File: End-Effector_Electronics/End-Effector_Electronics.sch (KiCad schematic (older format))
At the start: 23 parts, among them J1 Raspberry_Pi_2_3, J2 LynxServo, J3 QWIIC_Generic_Conn, J4 LynxServo, Q1 Q_PMOS_GSD, Q2 DMMT3906, Q3 Q_NMOS_GSD, U2 CAT24C32, U3 TDK_I3A4W008A033V

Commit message: Worked on finding components
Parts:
- C1: renamed from C5; footprint (none) -> Capacitor_SMD:CP_Elec_6.3x5.4; Digikey Part Num (none) -> PCE4244CT-ND
- C2: renamed from C6; footprint (none) -> Capacitor_SMD:C_0603_1608Metric
- C3: renamed from C7; footprint (none) -> Capacitor_SMD:CP_Elec_6.3x5.4; Digikey Part Num (none) -> 493-9805-1-ND
- H1, H2, H3, H4: footprint (none) -> MountingHole:MountingHole_2.7mm_M2.5_Pad
- renumbered J4 to J3, J3 to J4, R3 to R1, R4 to R2, R5 to R3, R6 to R4, R1 to R5, R2 to R6, U2 to U1, U3 to U2
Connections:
- net 12V_Disable: now also J1.36 (GPIO16)

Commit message: More component part selection
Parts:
- Q1: footprint (none) -> Package_TO_SOT_SMD:SOT-23
- Q2: footprint (none) -> Package_TO_SOT_SMD:SOT-23-6
- U1: footprint (none) -> Package_SO:TSSOP-8_4.4x3mm_P0.65mm
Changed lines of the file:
@@
 F 0 "U1" H 2950 7050 50  0000 C CNN
 F 1 "CAT24C32" H 2950 6950 50  0000 C CNN
-F 2 "" H 3250 6700 50  0001 C CNN
+F 2 "Package_SO:TSSOP-8_4.4x3mm_P0.65mm" H 3250 6700 50  0001 C CNN
 F 3 "http://ww1.microchip.com/downloads/en/DeviceDoc/21703d.pdf" H 3250 6700 50  0001 C CNN
 F 4 "CAT24C32YI-GT3OSCT-ND" H 3250 6700 50  0001 C CNN "Digikey Part Num"
@@
 F 0 "Q2" H 5113 6704 50  0000 R CNN
 F 1 "DMMT3906" H 5113 6795 50  0000 R CNN
-F 2 "" H 5400 6750 50  0001 C CIN
+F 2 "Package_TO_SOT_SMD:SOT-23-6" H 5400 6750 50  0001 C CIN
 F 3 "~" H 5500 6750 50  0001 L CNN
 F 4 "DMMT3906-7-FDICT-ND" H 5400 6750 50  0001 C CNN "Digikey Part Num"
@@
 F 0 "Q1" V 5742 6200 50  0000 C CNN
 F 1 "Q_PMOS_GSD" V 5651 6200 50  0000 C CNN
-F 2 "" H 5600 6300 50  0001 C CNN
+F 2 "Package_TO_SOT_SMD:SOT-23" H 5600 6300 50  0001 C CNN
 F 3 "~" H 5400 6200 50  0001 C CNN
 F 4 "TSM500P02CXRFGCT-ND" V 5400 6200 50  0001 C CNN "Digikey Part Num"

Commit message: Update End-Effector_Electronics.sch
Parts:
- J1: footprint (none) -> Connector_PinSocket_2.54mm:PinSocket_2x20_P2.54mm_Vertical; Digikey Part Num (none) -> 1528-1785-ND
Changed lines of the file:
@@
 F 0 "J1" H 2500 3950 50  0000 C CNN
 F 1 "Raspberry_Pi_2_3" H 2800 3850 50  0000 C CNN
-F 2 "" H 2150 2600 50  0001 C CNN
+F 2 "Connector_PinSocket_2.54mm:PinSocket_2x20_P2.54mm_Vertical" H 2150 2600 50  0001 C CNN
 F 3 "https://www.raspberrypi.org/documentation/hardware/raspberrypi/schematics/rpi_SCH_3bplus_1p0_reduced.pdf" H 2150 2600 50  0001 C CNN
+F 4 "1528-1785-ND" H 2150 2600 50  0001 C CNN "Digikey Part Num"
 	1    2150 2600
 	1    0    0    -1

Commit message: finished associating part nums and footprints
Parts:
- BT1: footprint (none) -> Connector_AMASS:AMASS_XT30PW-M_1x02_P2.50mm_Horizontal; Digikey Part Num (none) -> n/a
- H1, H2, H3, H4: Digikey Part Num (none) -> n/a
- J4: footprint (none) -> Connector_JST:JST_SH_BM04B-SRSS-TB_1x04-1MP_P1.00mm_Vertical; Digikey Part Num (none) -> n/a
- Q3: footprint (none) -> Package_TO_SOT_SMD:SOT-23; Digikey Part Num (none) -> DMN2041L-7DICT-ND
- R1, R2, R3: footprint (none) -> Resistor_SMD:R_0603_1608Metric
- R4: footprint (none) -> Resistor_SMD:R_0603_1608Metric; Digikey Part Num (none) -> 311-47.0KHRCT-ND
- R5: footprint (none) -> Resistor_SMD:R_0603_1608Metric; Digikey Part Num (none) -> 311-100KHRCT-ND
- R6: footprint (none) -> Resistor_SMD:R_0603_1608Metric; Digikey Part Num (none) -> RMCF0603FT1K82CT-ND
- U2: footprint (none) -> ASTRA_Footprints:Power_Supply_32nd_Brick; Digikey Part Num (none) -> I3A4W008A033V-001-R
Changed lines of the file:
@@
 F 0 "U2" H 7950 4765 50  0000 C CNN
 F 1 "TDK_I3A4W008A033V" H 7950 4674 50  0000 C CNN
-F 2 "" H 7450 4600 50  0001 C CNN
+F 2 "ASTRA_Footprints:Power_Supply_32nd_Brick" H 7450 4600 50  0001 C CNN
 F 3 "" H 7450 4600 50  0001 C CNN
+F 4 "I3A4W008A033V-001-R" H 7950 4300 50  0001 C CNN "Digikey Part Num"
 	1    7950 4300
 	1    0    0    -1
@@
 F 0 "J4" H 8178 1696 50  0000 L CNN
 F 1 "QWIIC_Generic_Conn" H 8178 1605 50  0000 L CNN
-F 2 "" H 8000 1950 50  0001 C CNN
+F 2 "Connector_JST:JST_SH_BM04B-SRSS-TB_1x04-1MP_P1.00mm_Vertical" H 8000 1950 50  0001 C CNN
 F 3 "" H 8000 1950 50  0001 C CNN
+F 4 "n/a" H 8000 1950 50  0001 C CNN "Digikey Part Num"
 	1    8000 1950
 	1    0    0    -1
@@
 F 0 "R6" H 8759 4446 50  0000 L CNN
 F 1 "1.82k" H 8759 4355 50  0000 L CNN
-F 2 "" H 8700 4400 50  0001 C CNN
+F 2 "Resistor_SMD:R_0603_1608Metric" H 8700 4400 50  0001 C CNN
 F 3 "~" H 8700 4400 50  0001 C CNN
+F 4 "RMCF0603FT1K82CT-ND" H 8700 4400 50  0001 C CNN "Digikey Part Num"
 	1    8700 4400
 	1    0    0    -1
@@
 F 0 "Q3" H 6806 4646 50  0000 L CNN
 F 1 "Q_NMOS_GSD" H 6806 4555 50  0000 L CNN
-F 2 "" H 6800 4700 50  0001 C CNN
+F 2 "Package_TO_SOT_SMD:SOT-23" H 6800 4700 50  0001 C CNN
 F 3 "~" H 6600 4600 50  0001 C CNN
+F 4 "DMN2041L-7DICT-ND" H 6600 4600 50  0001 C CNN "Digikey Part Num"
 	1    6600 4600
 	1    0    0    -1
@@
 F 0 "R5" H 6409 4846 50  0000 L CNN
 F 1 "100k" H 6409 4755 50  0000 L CNN
-F 2 "" H 6350 4800 50  0001 C CNN
+F 2 "Resistor_SMD:R_0603_1608Metric" H 6350 4800 50  0001 C CNN
 F 3 "~" H 6350 4800 50  0001 C CNN
+F 4 "311-100KHRCT-ND" H 6350 4800 50  0001 C CNN "Digikey Part Num"
 	1    6350 4800
 	1    0    0    -1
@@
 F 0 "BT1" H 1378 6896 50  0000 L CNN
 F 1 "XT_Battery_Connector" H 1378 6805 50  0000 L CNN
-F 2 "" H 1250 6850 50  0001 C CNN
+F 2 "Connector_AMASS:AMASS_XT30PW-M_1x02_P2.50mm_Horizontal" H 1250 6850 50  0001 C CNN
 F 3 "" H 1250 6850 50  0001 C CNN
+F 4 "n/a" H 1250 6850 50  0001 C CNN "Digikey Part Num"
 	1    1250 6850
 	1    0    0    -1
@@
 F 0 "R1" H 3759 7196 50  0000 L CNN
 F 1 "DNP" H 3759 7105 50  0000 L CNN
-F 2 "" H 3700 7150 50  0001 C CNN
+F 2 "Resistor_SMD:R_0603_1608Metric" H 3700 7150 50  0001 C CNN
 F 3 "~" H 3700 7150 50  0001 C CNN
 F 4 "n/a" H 3700 7150 50  0001 C CNN "Digikey Part Num"
@@
 F 0 "R2" V 3846 6800 50  0000 C CNN
 F 1 "10k" V 3755 6800 50  0000 C CNN
-F 2 "" H 3950 6800 50  0001 C CNN
+F 2 "Resistor_SMD:R_0603_1608Metric" H 3950 6800 50  0001 C CNN
 F 3 "~" H 3950 6800 50  0001 C CNN
 F 4 "n/a" H 3950 6800 50  0001 C CNN "Digikey Part Num"
@@
 F 0 "R3" H 5141 7154 50  0000 R CNN
 F 1 "10k" H 5141 7245 50  0000 R CNN
-F 2 "" H 5200 7200 50  0001 C CNN
+F 2 "Resistor_SMD:R_0603_1608Metric" H 5200 7200 50  0001 C CNN
 F 3 "~" H 5200 7200 50  0001 C CNN
 F 4 "n/a" H 5200 7200 50  0001 C CNN "Digikey Part Num"
@@
 F 0 "R4" H 5659 7246 50  0000 L CNN
 F 1 "47k" H 5659 7155 50  0000 L CNN
-F 2 "" H 5600 7200 50  0001 C CNN
+F 2 "Resistor_SMD:R_0603_1608Metric" H 5600 7200 50  0001 C CNN
 F 3 "~" H 5600 7200 50  0001 C CNN
+F 4 "311-47.0KHRCT-ND" H 5600 7200 50  0001 C CNN "Digikey Part Num"
 	1    5600 7200
 	1    0    0    -1
@@
 F 2 "MountingHole:MountingHole_2.7mm_M2.5_Pad" H 10000 950 50  0001 C CNN
 F 3 "~" H 10000 950 50  0001 C CNN
+F 4 "n/a" H 10000 950 50  0001 C CNN "Digikey Part Num"
 	1    10000 950
 	0    1    1    0
@@
 F 2 "MountingHole:MountingHole_2.7mm_M2.5_Pad" H 10000 1100 50  0001 C CNN
 F 3 "~" H 10000 1100 50  0001 C CNN
+F 4 "n/a" H 10000 1100 50  0001 C CNN "Digikey Part Num"
 	1    10000 1100
 	0    1    1    0
@@
 F 2 "MountingHole:MountingHole_2.7mm_M2.5_Pad" H 10000 1250 50  0001 C CNN
 F 3 "~" H 10000 1250 50  0001 C CNN
+F 4 "n/a" H 10000 1250 50  0001 C CNN "Digikey Part Num"
 	1    10000 1250
 	0    1    1    0
@@
 F 2 "MountingHole:MountingHole_2.7mm_M2.5_Pad" H 10000 1400 50  0001 C CNN
 F 3 "~" H 10000 1400 50  0001 C CNN
+F 4 "n/a" H 10000 1400 50  0001 C CNN "Digikey Part Num"
 	1    10000 1400
 	0    1    1    0

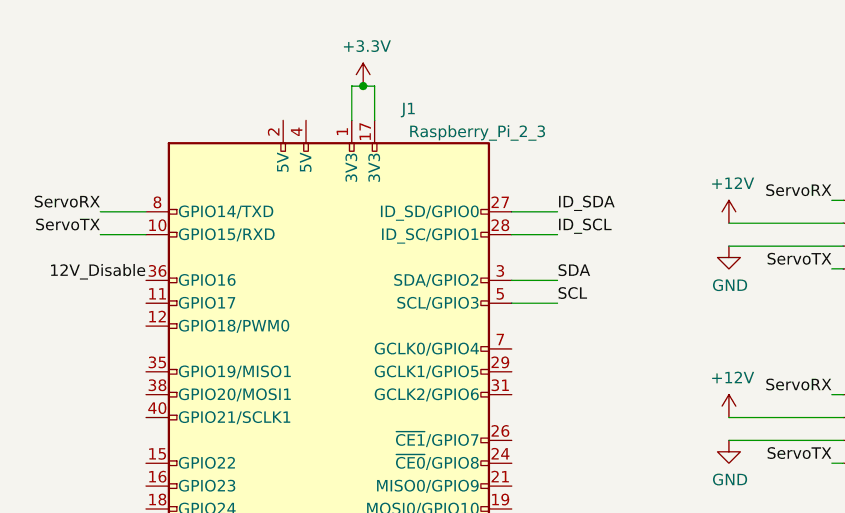
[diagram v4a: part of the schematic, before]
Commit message: Finished layout and routing of initial components
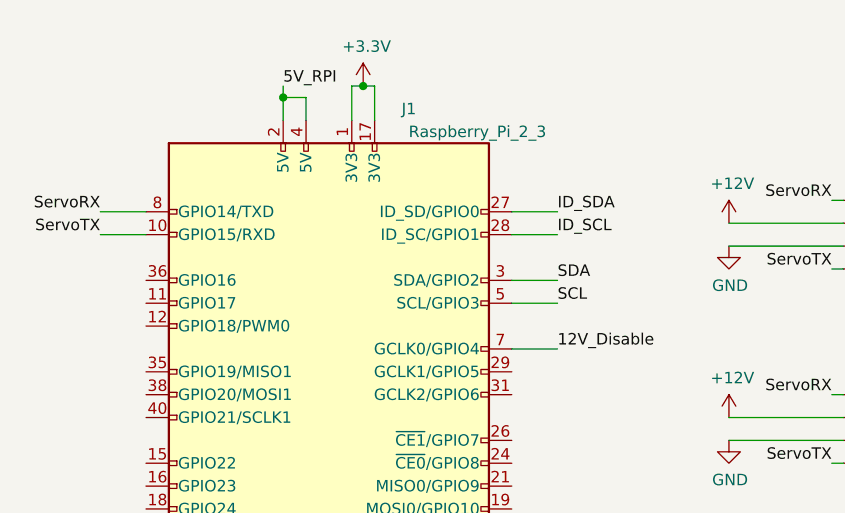
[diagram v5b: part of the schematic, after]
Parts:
- J1: footprint Connector_PinSocket_2.54mm:PinSocket_2x20_P2.54mm_Vertical -> Connector_PinSocket_2.54mm:PinSocket_2x20_P2.54mm_Vertical_SMD
- J4: footprint Connector_JST:JST_SH_BM04B-SRSS-TB_1x04-1MP_P1.00mm_Vertical -> Connector_JST:JST_SH_SM04B-SRSS-TB_1x04-1MP_P1.00mm_Horizontal
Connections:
- net 12V_Disable: now also J1.7 (GCLK0/GPIO4); no longer J1.36 (GPIO16)
- net 5V_RPI: now also J1.2 (5V), J1.4 (5V)
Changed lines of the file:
@@
 F 0 "J4" H 8178 1696 50  0000 L CNN
 F 1 "QWIIC_Generic_Conn" H 8178 1605 50  0000 L CNN
-F 2 "Connector_JST:JST_SH_BM04B-SRSS-TB_1x04-1MP_P1.00mm_Vertical" H 8000 1950 50  0001 C CNN
+F 2 "Connector_JST:JST_SH_SM04B-SRSS-TB_1x04-1MP_P1.00mm_Horizontal" H 8000 1950 50  0001 C CNN
 F 3 "" H 8000 1950 50  0001 C CNN
 F 4 "n/a" H 8000 1950 50  0001 C CNN "Digikey Part Num"
@@
 F 0 "J1" H 2500 3950 50  0000 C CNN
 F 1 "Raspberry_Pi_2_3" H 2800 3850 50  0000 C CNN
-F 2 "Connector_PinSocket_2.54mm:PinSocket_2x20_P2.54mm_Vertical" H 2150 2600 50  0001 C CNN
+F 2 "Connector_PinSocket_2.54mm:PinSocket_2x20_P2.54mm_Vertical_SMD" H 2150 2600 50  0001 C CNN
 F 3 "https://www.raspberrypi.org/documentation/hardware/raspberrypi/schematics/rpi_SCH_3bplus_1p0_reduced.pdf" H 2150 2600 50  0001 C CNN
 F 4 "1528-1785-ND" H 2150 2600 50  0001 C CNN "Digikey Part Num"
@@
 	0    1    1    0
 $EndComp
-Text Label 1350 2000 2    50   ~ 0
+Text Label 3150 2300 0    50   ~ 0
 12V_Disable
+Text Label 1950 1150 0    50   ~ 0
+5V_RPI
+Wire Wire Line
+	2050 1300 2050 1200
+Wire Wire Line
+	2050 1200 1950 1200
+Wire Wire Line
+	1950 1200 1950 1150
+Wire Wire Line
+	1950 1200 1950 1300
+Connection ~ 1950 1200
+Wire Wire Line
+	3150 2300 2950 2300
 $EndSCHEMATC

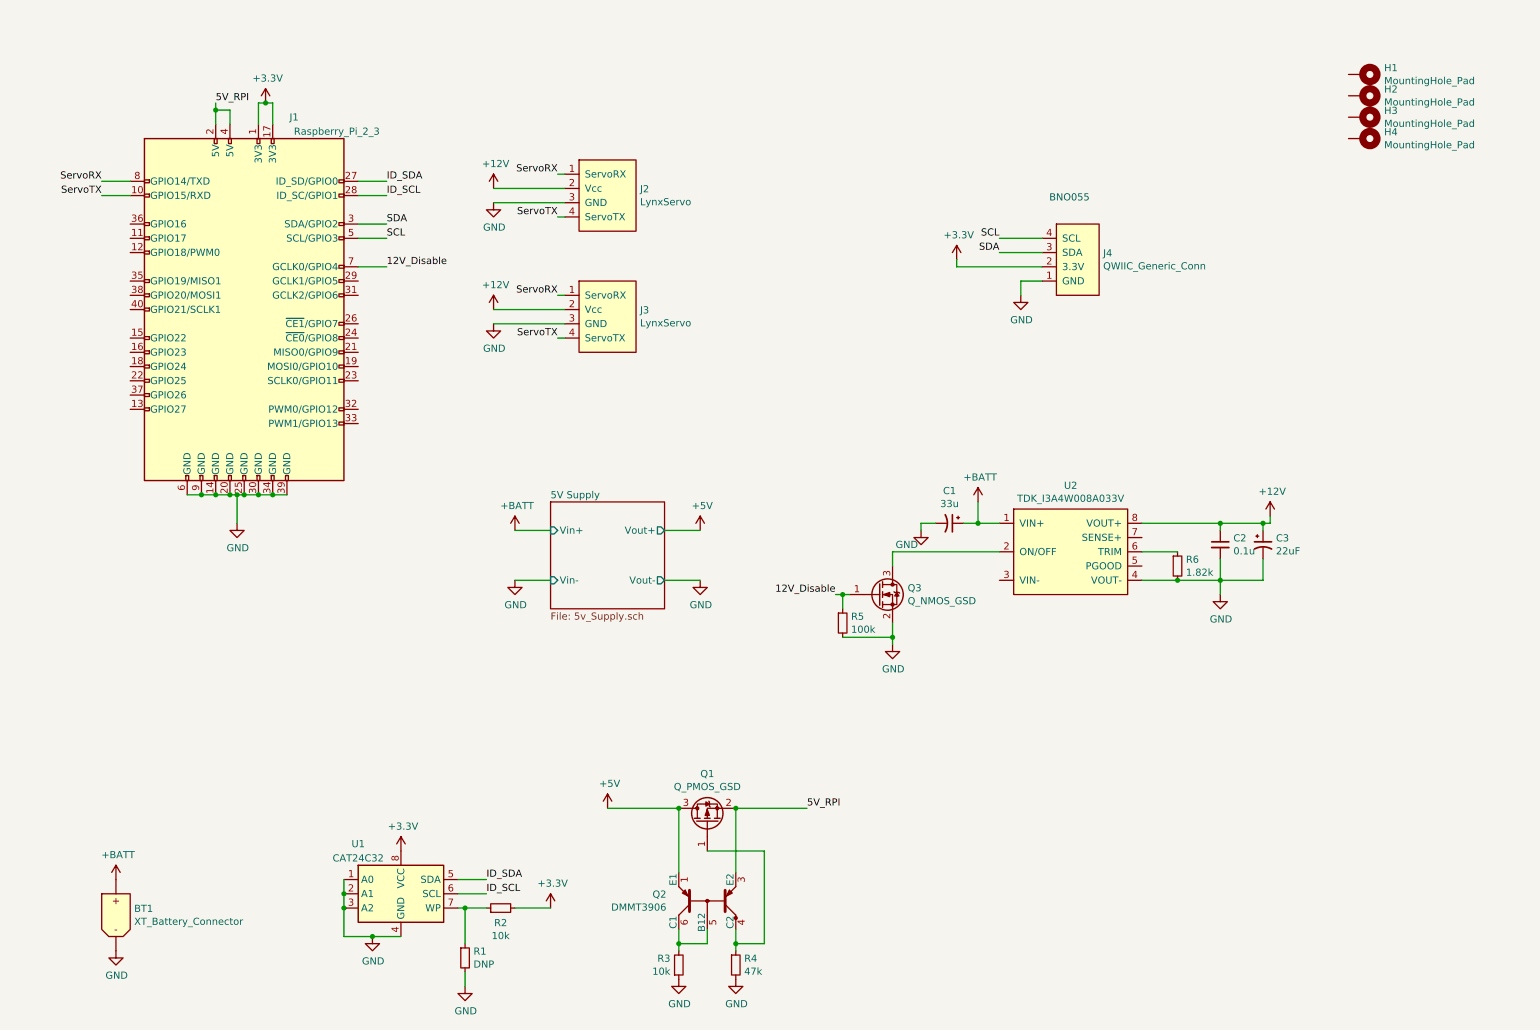
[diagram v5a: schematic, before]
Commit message: added things and cleaned up silkscreen
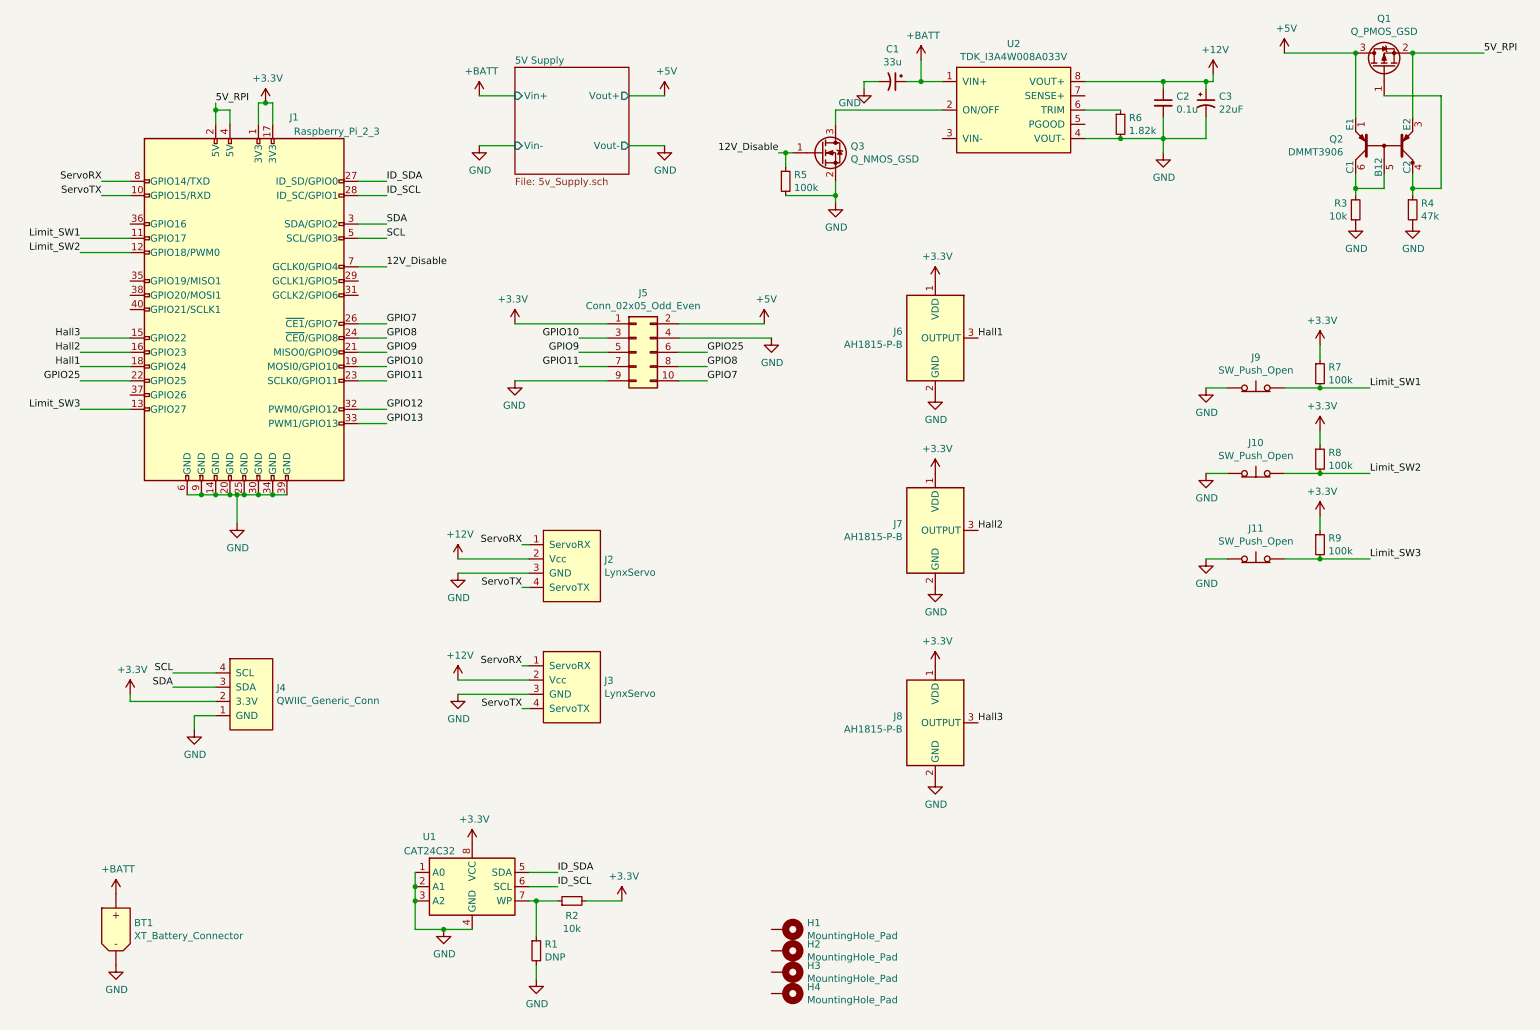
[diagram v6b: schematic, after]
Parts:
- added J10, J11, J9: SW_Push_Open, Connector_JST:JST_PH_B2B-PH-K_1x02_P2.00mm_Vertical, symbol Switch:SW_Push_Open
- added J5: Conn_02x05_Odd_Even, Connector_PinHeader_2.54mm:PinHeader_2x05_P2.54mm_Vertical_SMD, symbol Connector_Generic:Conn_02x05_Odd_Even
- added J6, J7, J8: AH1815-P-B, Connector_JST:JST_PH_B3B-PH-K_1x03_P2.00mm_Vertical, symbol Project_Library:AH1815-P-B
- added R7, R8, R9: 100k, Resistor_SMD:R_0603_1608Metric, symbol Device:R_Small
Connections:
- net +3V3: now also J5.1 (Pin_1), J6.1 (VDD), J7.1 (VDD), J8.1 (VDD), R7.1, R8.1, R9.1
- net +5V: now also J5.2 (Pin_2)
- net GND: now also J10.1 (A), J11.1 (A), J5.4 (Pin_4), J5.9 (Pin_9), J6.2 (GND), J7.2 (GND), J8.2 (GND), J9.1 (A)
- net Limit_SW1: now reaches J1.11 (GPIO17)
- net Limit_SW1: now also J9.2 (B), R7.2
- net Limit_SW2: now reaches J1.12 (GPIO18/PWM0)
- net Limit_SW2: now also J10.2 (B), R8.2
- net Limit_SW3: now reaches J1.13 (GPIO27)
- net Limit_SW3: now also J11.2 (B), R9.2
- net Hall3: now reaches J1.15 (GPIO22)
- net Hall3: now also J8.3 (OUTPUT)
- net Hall2: now reaches J1.16 (GPIO23)
- net Hall2: now also J7.3 (OUTPUT)
- net Hall1: now reaches J1.18 (GPIO24)
- net Hall1: now also J6.3 (OUTPUT)
- net GPIO10: now reaches J1.19 (MOSI0/GPIO10)
- net GPIO10: now also J5.3 (Pin_3)
- net GPIO9: now reaches J1.21 (MISO0/GPIO9)
- net GPIO9: now also J5.5 (Pin_5)
- net GPIO25: now reaches J1.22 (GPIO25)
- net GPIO25: now also J5.6 (Pin_6)
- net GPIO11: now reaches J1.23 (SCLK0/GPIO11)
- net GPIO11: now also J5.7 (Pin_7)
- net GPIO8: now reaches J1.24 (~CE0~/GPIO8)
- net GPIO8: now also J5.8 (Pin_8)
- net GPIO7: now reaches J1.26 (~CE1~/GPIO7)
- net GPIO7: now also J5.10 (Pin_10)
- net GPIO12: now reaches J1.32 (PWM0/GPIO12)
- net GPIO13: now reaches J1.33 (PWM1/GPIO13)
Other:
- note removed: "BNO055"
- moved on the sheet: BT1, C1, C2, C3, H1, H2, H3, H4, J2, J3, J4, Q1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
